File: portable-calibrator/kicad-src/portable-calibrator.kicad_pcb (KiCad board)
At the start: 2 copper layers, 30.7 x 26.7 mm, 15 parts, among them J1 Conn_01x02, J2 Conn_01x02, Q1 MMBT3904-7-F, U1 LM399, U2 LT1012

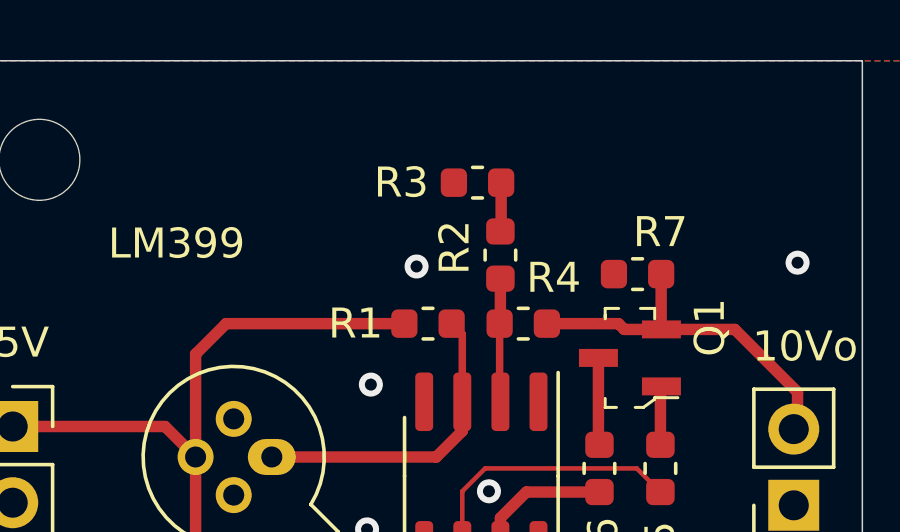
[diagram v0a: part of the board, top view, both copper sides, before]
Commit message: reroute portable calibrator
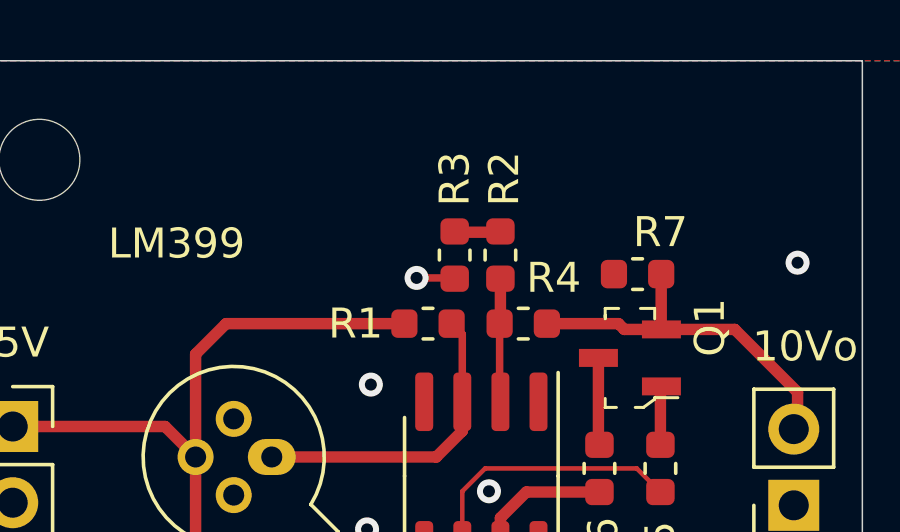
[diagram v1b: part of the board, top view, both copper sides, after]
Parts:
- moved R3 2.53 mm to (157.1, 90.3), turned to 90 degrees
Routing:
- net GND: track 0.00 -> 1.28 mm
